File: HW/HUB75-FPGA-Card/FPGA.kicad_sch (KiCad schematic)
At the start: 40 parts, among them J1 Conn_02x04_Odd_Even, U1 AMS1117-3.3, U2 AP2112K-1.2, U3 T20Q100F3, X1 ECS-2520MV-xxx-xx

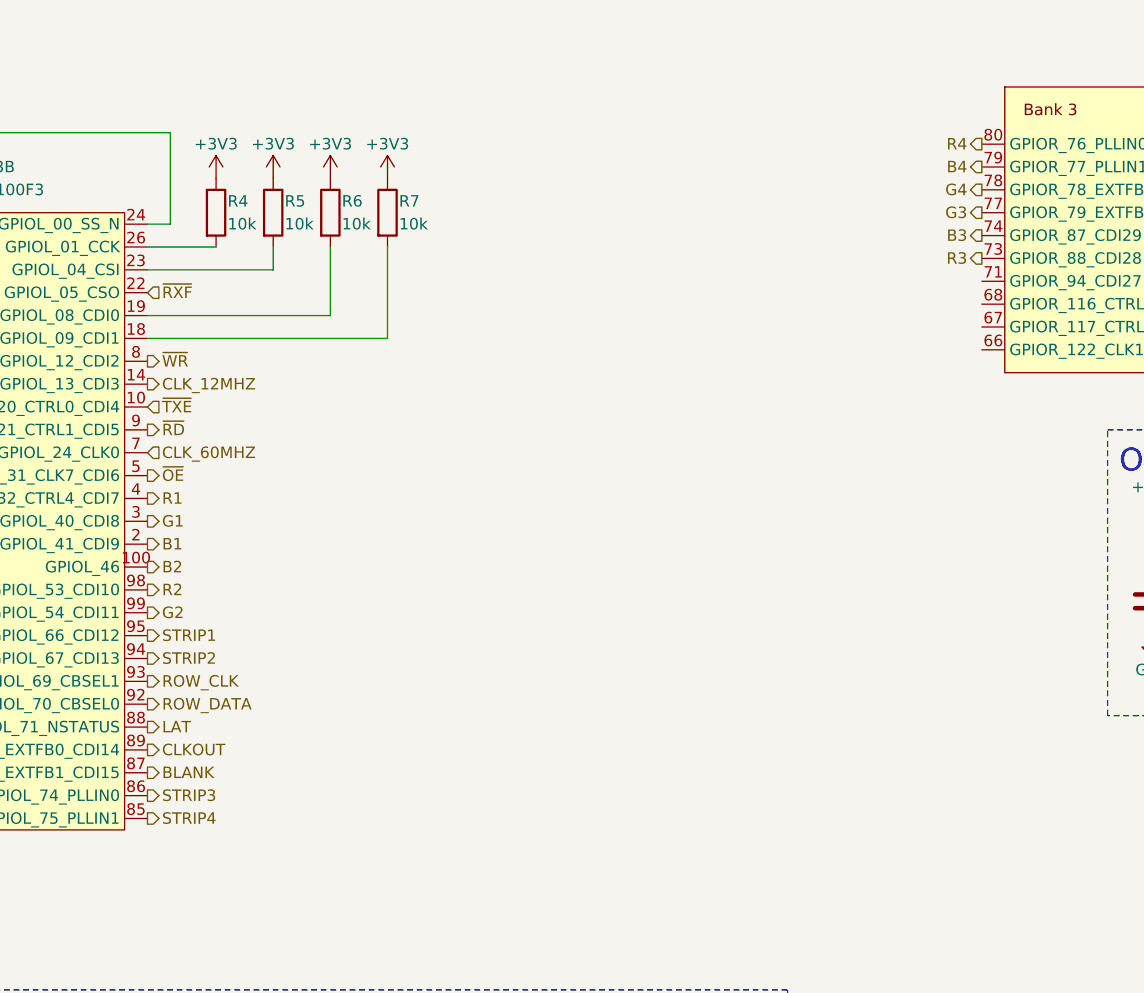
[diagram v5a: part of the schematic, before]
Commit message: update components and generate production files
still need to look into CBSEL
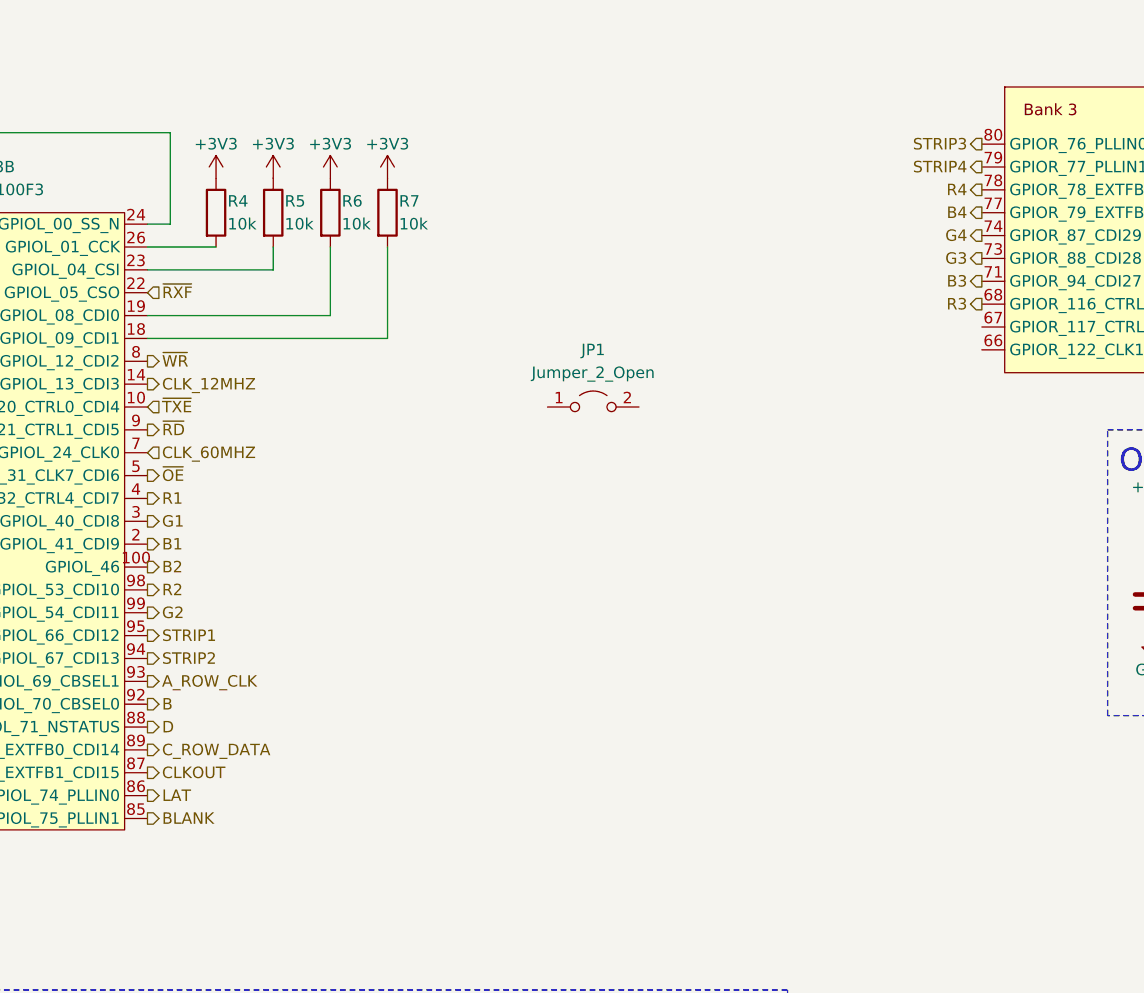
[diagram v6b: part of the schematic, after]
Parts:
- added JP1: Jumper_2_Open, symbol Jumper:Jumper_2_Open
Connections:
- net B3: now also U3.71 (GPIOR_94_CDI27); no longer U3.74 (GPIOR_87_CDI29)
- net B4: now also U3.77 (GPIOR_79_EXTFB1_CDI30); no longer U3.79 (GPIOR_77_PLLIN1)
- net BLANK: now also U3.85 (GPIOL_75_PLLIN1); no longer U3.87 (GPIOL_73_EXTFB1_CDI15)
- net CLKOUT: now also U3.87 (GPIOL_73_EXTFB1_CDI15); no longer U3.89 (GPIOL_72_EXTFB0_CDI14)
- net G3: now also U3.73 (GPIOR_88_CDI28); no longer U3.77 (GPIOR_79_EXTFB1_CDI30)
- net G4: now also U3.74 (GPIOR_87_CDI29); no longer U3.78 (GPIOR_78_EXTFB0_CDI31)
- net LAT: now also U3.86 (GPIOL_74_PLLIN0); no longer U3.88 (GPIOL_71_NSTATUS)
- net R3: now also U3.68 (GPIOR_116_CTRL15); no longer U3.73 (GPIOR_88_CDI28)
- net R4: now also U3.78 (GPIOR_78_EXTFB0_CDI31); no longer U3.80 (GPIOR_76_PLLIN0)
- net STRIP3: now also U3.80 (GPIOR_76_PLLIN0); no longer U3.86 (GPIOL_74_PLLIN0)
- net STRIP4: now also U3.79 (GPIOR_77_PLLIN1); no longer U3.85 (GPIOL_75_PLLIN1)
- net ROW_CLK renamed A_ROW_CLK
- net ROW_DATA renamed B
- new net C_ROW_DATA: U3.89 (GPIOL_72_EXTFB0_CDI14)
- new net D: U3.88 (GPIOL_71_NSTATUS)
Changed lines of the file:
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@@
     (effects (font (size 1.27 1.27)) (justify left))
   )
-  (hierarchical_label "CLKOUT" (shape output) (at 100.33 96.52 0) (fields_autoplaced)
-    (effects (font (size 1.27 1.27)) (justify left))
-  )
-  (hierarchical_label "ROW_DATA" (shape output) (at 100.33 91.44 0) (fields_autoplaced)
+  (hierarchical_label "CLKOUT" (shape output) (at 100.33 99.06 0) (fields_autoplaced)
+    (effects (font (size 1.27 1.27)) (justify left))
+  )
+  (hierarchical_label "C_ROW_DATA" (shape output) (at 100.33 96.52 0) (fields_autoplaced)
     (effects (font (size 1.27 1.27)) (justify left))
   )
@@
     (effects (font (size 1.27 1.27)) (justify left))
   )
-  (hierarchical_label "LAT" (shape output) (at 100.33 93.98 0) (fields_autoplaced)
+  (hierarchical_label "LAT" (shape output) (at 100.33 101.6 0) (fields_autoplaced)
     (effects (font (size 1.27 1.27)) (justify left))
   )
@@
     (effects (font (size 1.27 1.27)) (justify left))
   )
-  (hierarchical_label "R4" (shape output) (at 193.04 29.21 180) (fields_autoplaced)
+  (hierarchical_label "R4" (shape output) (at 193.04 34.29 180) (fields_autoplaced)
     (effects (font (size 1.27 1.27)) (justify right))
   )
@@
     (effects (font (size 1.27 1.27)) (justify left))
   )
-  (hierarchical_label "R3" (shape output) (at 193.04 41.91 180) (fields_autoplaced)
+  (hierarchical_label "R3" (shape output) (at 193.04 46.99 180) (fields_autoplaced)
     (effects (font (size 1.27 1.27)) (justify right))
   )
@@
     (effects (font (size 1.27 1.27)) (justify left))
   )
-  (hierarchical_label "BLANK" (shape output) (at 100.33 99.06 0) (fields_autoplaced)
-    (effects (font (size 1.27 1.27)) (justify left))
-  )
-  (hierarchical_label "STRIP4" (shape output) (at 100.33 104.14 0) (fields_autoplaced)
-    (effects (font (size 1.27 1.27)) (justify left))
-  )
-  (hierarchical_label "STRIP3" (shape output) (at 100.33 101.6 0) (fields_autoplaced)
-    (effects (font (size 1.27 1.27)) (justify left))
-  )
-  (hierarchical_label "B4" (shape output) (at 193.04 31.75 180) (fields_autoplaced)
+  (hierarchical_label "BLANK" (shape output) (at 100.33 104.14 0) (fields_autoplaced)
+    (effects (font (size 1.27 1.27)) (justify left))
+  )
+  (hierarchical_label "STRIP4" (shape output) (at 193.04 31.75 180) (fields_autoplaced)
     (effects (font (size 1.27 1.27)) (justify right))
   )
+  (hierarchical_label "B" (shape output) (at 100.33 91.44 0) (fields_autoplaced)
+    (effects (font (size 1.27 1.27)) (justify left))
+  )
+  (hierarchical_label "STRIP3" (shape output) (at 193.04 29.21 180) (fields_autoplaced)
+    (effects (font (size 1.27 1.27)) (justify right))
+  )
+  (hierarchical_label "B4" (shape output) (at 193.04 36.83 180) (fields_autoplaced)
+    (effects (font (size 1.27 1.27)) (justify right))
+  )
   (hierarchical_label "D5" (shape input) (at 248.92 134.62 0) (fields_autoplaced)
     (effects (font (size 1.27 1.27)) (justify left))
   )
-  (hierarchical_label "ROW_CLK" (shape output) (at 100.33 88.9 0) (fields_autoplaced)
+  (hierarchical_label "D" (shape output) (at 100.33 93.98 0) (fields_autoplaced)
+    (effects (font (size 1.27 1.27)) (justify left))
+  )
+  (hierarchical_label "A_ROW_CLK" (shape output) (at 100.33 88.9 0) (fields_autoplaced)
     (effects (font (size 1.27 1.27)) (justify left))
   )
@@
     (effects (font (size 1.27 1.27)) (justify left))
   )
-  (hierarchical_label "G4" (shape output) (at 193.04 34.29 180) (fields_autoplaced)
+  (hierarchical_label "G4" (shape output) (at 193.04 39.37 180) (fields_autoplaced)
     (effects (font (size 1.27 1.27)) (justify right))
   )
@@
     (effects (font (size 1.27 1.27)) (justify left))
   )
-  (hierarchical_label "G3" (shape output) (at 193.04 36.83 180) (fields_autoplaced)
+  (hierarchical_label "G3" (shape output) (at 193.04 41.91 180) (fields_autoplaced)
     (effects (font (size 1.27 1.27)) (justify right))
   )
-  (hierarchical_label "B3" (shape output) (at 193.04 39.37 180) (fields_autoplaced)
+  (hierarchical_label "B3" (shape output) (at 193.04 44.45 180) (fields_autoplaced)
     (effects (font (size 1.27 1.27)) (justify right))
   )
@@
         )
       )
+    )
+  )
+  (symbol (lib_id "Jumper:Jumper_2_Open") (at 149.86 58.42 0) (unit 1)
+    (in_bom yes) (on_board yes) (dnp no) (fields_autoplaced)
+    (property "Reference" "JP1" (at 149.86 52.07 0)
+      (effects (font (size 1.27 1.27)))
+    )
+    (property "Value" "Jumper_2_Open" (at 149.86 54.61 0)
+      (effects (font (size 1.27 1.27)))
+    )
+    (property "Footprint" "" (at 149.86 58.42 0)
+      (effects (font (size 1.27 1.27)) hide)
+    )
+    (property "Datasheet" "~" (at 149.86 58.42 0)
+      (effects (font (size 1.27 1.27)) hide)
+    )
+    (pin "2")
+    (pin "1")
+    (instances
+      (project "HUB75-FPGA-Card"
+        (path "/12c1dc17-a9d4-409d-a42e-fc131eeff0fd/45acbd2b-2398-4f26-b8e7-9bd133bc66a8"
+          (reference "JP1") (unit 1)
+        )
+      )

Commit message: initial design for sbc 5v power board
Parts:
- added R23, R24: 10k, Resistor_SMD:R_0603_1608Metric, symbol Device:R
- JP1: footprint (none) -> Connector_PinHeader_2.54mm:PinHeader_1x02_P2.54mm_Vertical
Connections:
- net +3V3: now also JP1.2 (B)
- net A_ROW_CLK: now also U3.89 (GPIOL_72_EXTFB0_CDI14); no longer U3.93 (GPIOL_69_CBSEL1)
- net B: now also U3.88 (GPIOL_71_NSTATUS); no longer U3.92 (GPIOL_70_CBSEL0)
- net B3: now also U3.67 (GPIOR_117_CTRL14); no longer U3.71 (GPIOR_94_CDI27)
- net B4: now also U3.73 (GPIOR_88_CDI28); no longer U3.77 (GPIOR_79_EXTFB1_CDI30)
- net BLANK: now also U3.79 (GPIOR_77_PLLIN1); no longer U3.85 (GPIOL_75_PLLIN1)
- net CLKOUT: now also U3.85 (GPIOL_75_PLLIN1); no longer U3.87 (GPIOL_73_EXTFB1_CDI15)
- net C_ROW_DATA: now also U3.87 (GPIOL_73_EXTFB1_CDI15); no longer U3.89 (GPIOL_72_EXTFB0_CDI14)
- net D: now also U3.86 (GPIOL_74_PLLIN0); no longer U3.88 (GPIOL_71_NSTATUS)
- net G3: now also U3.68 (GPIOR_116_CTRL15); no longer U3.73 (GPIOR_88_CDI28)
- net G4: now also U3.71 (GPIOR_94_CDI27); no longer U3.74 (GPIOR_87_CDI29)
- net GND: now also R23.2, R24.2
- net LAT: now also U3.80 (GPIOR_76_PLLIN0); no longer U3.86 (GPIOL_74_PLLIN0)
- net R3: now also U3.66 (GPIOR_122_CLK13_CDI21); no longer U3.68 (GPIOR_116_CTRL15)
- net R4: now also U3.74 (GPIOR_87_CDI29); no longer U3.78 (GPIOR_78_EXTFB0_CDI31)
- net STRIP3: now also U3.78 (GPIOR_78_EXTFB0_CDI31); no longer U3.80 (GPIOR_76_PLLIN0)
- net STRIP4: now also U3.77 (GPIOR_79_EXTFB1_CDI30); no longer U3.79 (GPIOR_77_PLLIN1)
- net at JP1.1 (A): now also U3.92 (GPIOL_70_CBSEL0), R24.1
- new net: R23.1, U3.93 (GPIOL_69_CBSEL1)
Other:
- note added: "Image Select"
- moved on the sheet: JP1
